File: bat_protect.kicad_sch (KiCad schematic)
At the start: 16 parts, among them Q9 Q_NMOS_DGS, U14 BQ29209DRBR

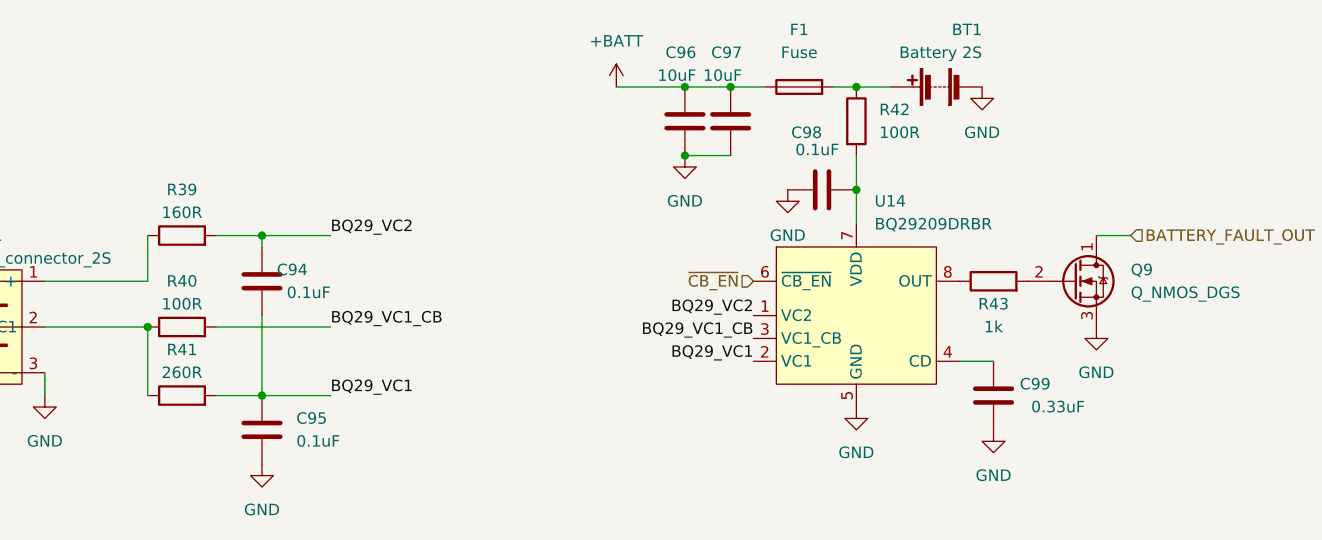
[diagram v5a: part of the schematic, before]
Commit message: datasheet checkout, added couple of capacitors for usb-c, groupd some scheatics
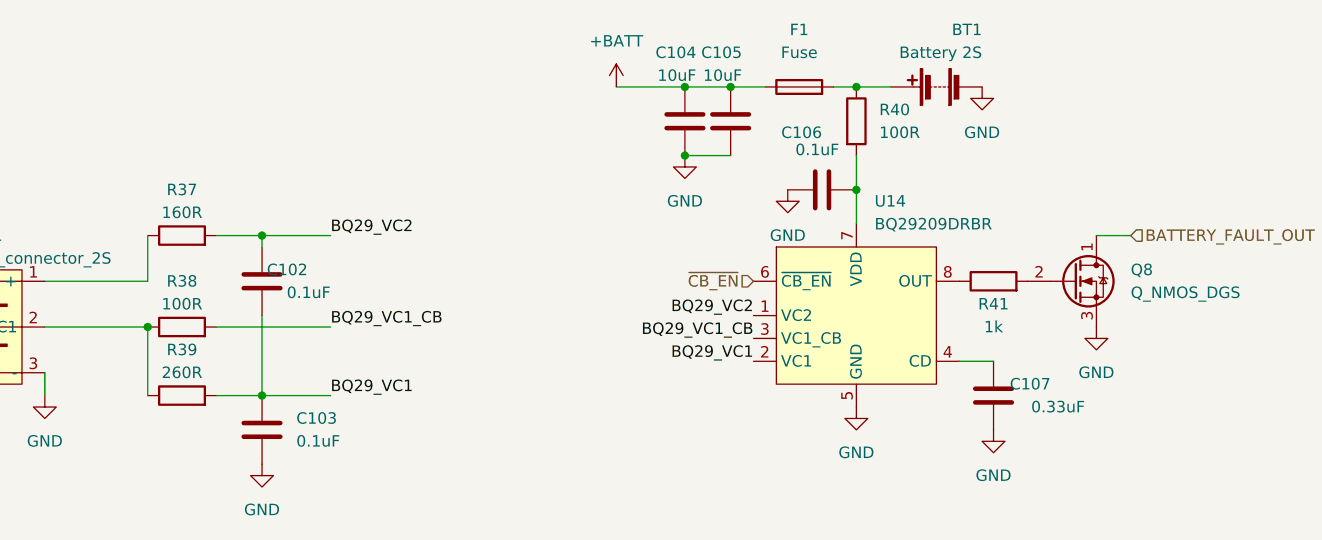
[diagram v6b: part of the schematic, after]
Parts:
- renumbered C94 to C102, C95 to C103, C96 to C104, C97 to C105, C98 to C106, C99 to C107, Q9 to Q8, R39 to R37, R40 to R38, R41 to R39, R42 to R40, R43 to R41
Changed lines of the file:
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@@
   (symbol (lib_id "power:GND") (at 78.74 99.06 0) (unit 1)
     (in_bom yes) (on_board yes) (fields_autoplaced)
-    (property "Reference" "#PWR0117" (id 0) (at 78.74 105.41 0)
+    (property "Reference" "#PWR0118" (id 0) (at 78.74 105.41 0)
       (effects (font (size 1.27 1.27)) hide)
     )
@@
   (symbol (lib_id "Device:R") (at 93.98 91.44 90) (unit 1)
     (in_bom yes) (on_board yes)
-    (property "Reference" "R40" (id 0) (at 93.98 86.36 90))
+    (property "Reference" "R38" (id 0) (at 93.98 86.36 90))
     (property "Value" "100R" (id 1) (at 93.98 88.9 90))
     (property "Footprint" "" (id 2) (at 93.98 93.218 90)
@@
   (symbol (lib_id "power:+BATT") (at 142.24 64.77 0) (unit 1)
     (in_bom yes) (on_board yes) (fields_autoplaced)
-    (property "Reference" "#PWR0119" (id 0) (at 142.24 68.58 0)
+    (property "Reference" "#PWR0120" (id 0) (at 142.24 68.58 0)
       (effects (font (size 1.27 1.27)) hide)
     )
@@
   (symbol (lib_id "power:GND") (at 102.87 106.68 0) (unit 1)
     (in_bom yes) (on_board yes) (fields_autoplaced)
-    (property "Reference" "#PWR0118" (id 0) (at 102.87 113.03 0)
+    (property "Reference" "#PWR0119" (id 0) (at 102.87 113.03 0)
       (effects (font (size 1.27 1.27)) hide)
     )
@@
   (symbol (lib_id "power:GND") (at 168.91 100.33 0) (unit 1)
     (in_bom yes) (on_board yes) (fields_autoplaced)
-    (property "Reference" "#PWR0122" (id 0) (at 168.91 106.68 0)
+    (property "Reference" "#PWR0123" (id 0) (at 168.91 106.68 0)
       (effects (font (size 1.27 1.27)) hide)
     )
@@
   (symbol (lib_id "power:GND") (at 149.86 72.39 0) (unit 1)
     (in_bom yes) (on_board yes) (fields_autoplaced)
-    (property "Reference" "#PWR0120" (id 0) (at 149.86 78.74 0)
+    (property "Reference" "#PWR0121" (id 0) (at 149.86 78.74 0)
       (effects (font (size 1.27 1.27)) hide)
     )
@@
   (symbol (lib_id "power:GND") (at 182.88 64.77 0) (unit 1)
     (in_bom yes) (on_board yes) (fields_autoplaced)
-    (property "Reference" "#PWR0123" (id 0) (at 182.88 71.12 0)
+    (property "Reference" "#PWR0124" (id 0) (at 182.88 71.12 0)
       (effects (font (size 1.27 1.27)) hide)
     )
@@
   (symbol (lib_id "Device:R") (at 93.98 81.28 90) (unit 1)
     (in_bom yes) (on_board yes)
-    (property "Reference" "R39" (id 0) (at 93.98 76.2 90))
+    (property "Reference" "R37" (id 0) (at 93.98 76.2 90))
     (property "Value" "160R" (id 1) (at 93.98 78.74 90))
     (property "Footprint" "" (id 2) (at 93.98 83.058 90)
@@
   (symbol (lib_id "power:GND") (at 161.29 76.2 0) (unit 1)
     (in_bom yes) (on_board yes) (fields_autoplaced)
-    (property "Reference" "#PWR0121" (id 0) (at 161.29 82.55 0)
+    (property "Reference" "#PWR0122" (id 0) (at 161.29 82.55 0)
       (effects (font (size 1.27 1.27)) hide)
     )
@@
   (symbol (lib_id "Device:C") (at 184.15 99.06 0) (mirror x) (unit 1)
     (in_bom yes) (on_board yes)
-    (property "Reference" "C99" (id 0) (at 190.5 97.79 0)
+    (property "Reference" "C107" (id 0) (at 190.5 97.79 0)
       (effects (font (size 1.27 1.27)) (justify right))
     )
@@
   (symbol (lib_id "Device:R") (at 184.15 86.36 90) (unit 1)
     (in_bom yes) (on_board yes)
-    (property "Reference" "R43" (id 0) (at 184.15 88.9 90))
+    (property "Reference" "R41" (id 0) (at 184.15 88.9 90))
     (property "Value" "1k" (id 1) (at 184.15 91.44 90))
     (property "Footprint" "" (id 2) (at 184.15 88.138 90)
@@
   (symbol (lib_id "Device:Q_NMOS_DGS") (at 193.04 86.36 0) (unit 1)
     (in_bom yes) (on_board yes) (fields_autoplaced)
-    (property "Reference" "Q9" (id 0) (at 199.39 85.0899 0)
+    (property "Reference" "Q8" (id 0) (at 199.39 85.0899 0)
       (effects (font (size 1.27 1.27)) (justify left))
     )
@@
   (symbol (lib_id "Device:C") (at 102.87 102.87 0) (mirror y) (unit 1)
     (in_bom yes) (on_board yes)
-    (property "Reference" "C95" (id 0) (at 106.68 101.6 0)
+    (property "Reference" "C103" (id 0) (at 106.68 101.6 0)
       (effects (font (size 1.27 1.27)) (justify right))
     )
@@
   (symbol (lib_id "power:GND") (at 195.58 91.44 0) (unit 1)
     (in_bom yes) (on_board yes) (fields_autoplaced)
-    (property "Reference" "#PWR0125" (id 0) (at 195.58 97.79 0)
+    (property "Reference" "#PWR0126" (id 0) (at 195.58 97.79 0)
       (effects (font (size 1.27 1.27)) hide)
     )
@@
   (symbol (lib_id "power:GND") (at 184.15 102.87 0) (unit 1)
     (in_bom yes) (on_board yes) (fields_autoplaced)
-    (property "Reference" "#PWR0124" (id 0) (at 184.15 109.22 0)
+    (property "Reference" "#PWR0125" (id 0) (at 184.15 109.22 0)
       (effects (font (size 1.27 1.27)) hide)
     )
@@
   (symbol (lib_id "Device:C") (at 149.86 68.58 0) (mirror x) (unit 1)
     (in_bom yes) (on_board yes)
-    (property "Reference" "C96" (id 0) (at 151.13 60.96 0)
+    (property "Reference" "C104" (id 0) (at 151.13 60.96 0)
       (effects (font (size 1.27 1.27)) (justify right))
     )
@@
   (symbol (lib_id "Device:C") (at 154.94 68.58 0) (mirror x) (unit 1)
     (in_bom yes) (on_board yes)
-    (property "Reference" "C97" (id 0) (at 156.21 60.96 0)
+    (property "Reference" "C105" (id 0) (at 156.21 60.96 0)
       (effects (font (size 1.27 1.27)) (justify right))
     )
@@
   (symbol (lib_id "Device:C") (at 165.1 76.2 270) (mirror x) (unit 1)
     (in_bom yes) (on_board yes)
-    (property "Reference" "C98" (id 0) (at 165.1 69.85 90)
+    (property "Reference" "C106" (id 0) (at 165.1 69.85 90)
       (effects (font (size 1.27 1.27)) (justify right))
     )
@@
   (symbol (lib_id "Device:C") (at 102.87 86.36 0) (mirror x) (unit 1)
     (in_bom yes) (on_board yes)
-    (property "Reference" "C94" (id 0) (at 107.95 85.09 0)
+    (property "Reference" "C102" (id 0) (at 107.95 85.09 0)
       (effects (font (size 1.27 1.27)) (justify right))
     )
@@
   (symbol (lib_id "Device:R") (at 93.98 99.06 90) (unit 1)
     (in_bom yes) (on_board yes)
-    (property "Reference" "R41" (id 0) (at 93.98 93.98 90))
+    (property "Reference" "R39" (id 0) (at 93.98 93.98 90))
     (property "Value" "260R" (id 1) (at 93.98 96.52 90))
     (property "Footprint" "" (id 2) (at 93.98 100.838 90)
@@
   (symbol (lib_id "Device:R") (at 168.91 68.58 0) (unit 1)
     (in_bom yes) (on_board yes) (fields_autoplaced)
-    (property "Reference" "R42" (id 0) (at 171.45 67.3099 0)
-      (effects (font (size 1.27 1.27)) (justify left))
-    )
+    (property "Reference" "R40" (id 0) (at 171.45 67.3099 0)
+      (effects (font (size 1.27 1.27)) (justify left))
+    )

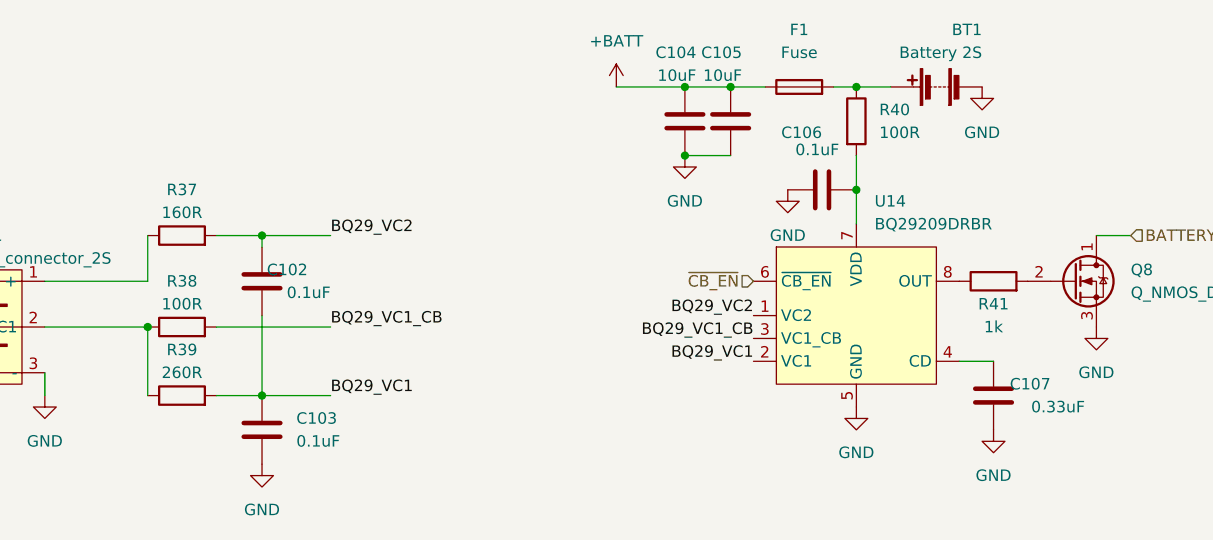
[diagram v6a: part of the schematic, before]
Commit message: added nfc antenna components, added most of footprints
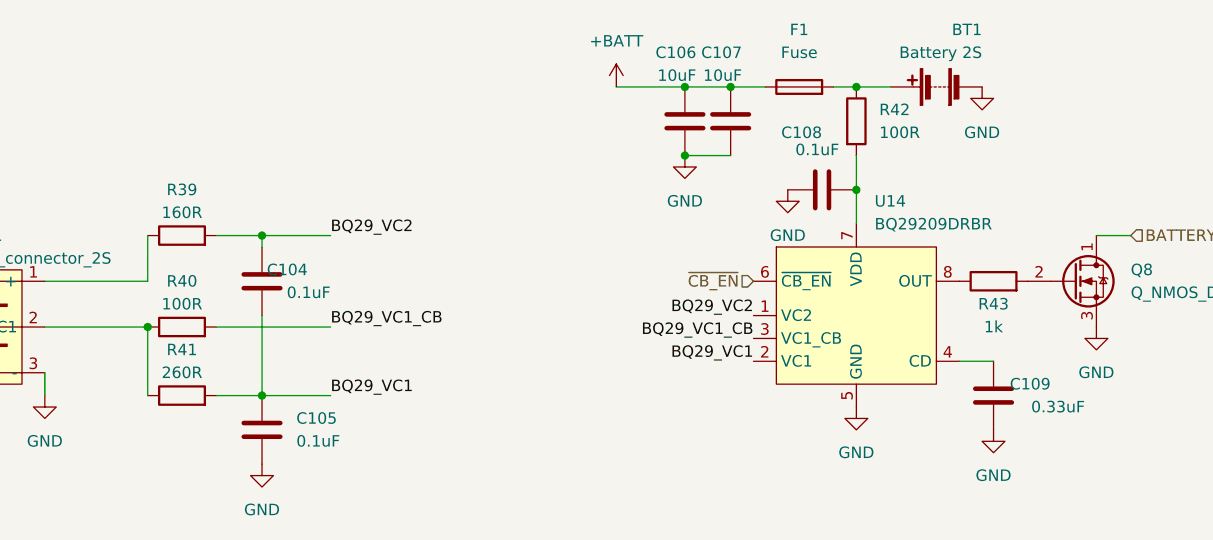
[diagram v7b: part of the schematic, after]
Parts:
- C104: renamed from C102; footprint (none) -> Capacitor_SMD:C_0603_1608Metric_Pad1.08x0.95mm_HandSolder
- C105: renamed from C103; footprint (none) -> Capacitor_SMD:C_0603_1608Metric_Pad1.08x0.95mm_HandSolder
- C108: renamed from C106; footprint (none) -> Capacitor_SMD:C_0603_1608Metric_Pad1.08x0.95mm_HandSolder
- C109: renamed from C107; footprint (none) -> Capacitor_SMD:C_0603_1608Metric_Pad1.08x0.95mm_HandSolder
- R42: renamed from R40; footprint (none) -> Resistor_SMD:R_0603_1608Metric_Pad0.98x0.95mm_HandSolder
- R43: renamed from R41; footprint (none) -> Resistor_SMD:R_0603_1608Metric_Pad0.98x0.95mm_HandSolder
- U14: footprint (none) -> airsoft_controller:VSON-8
- renumbered C104 to C106, C105 to C107, R37 to R39, R38 to R40, R39 to R41
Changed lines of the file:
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@@
   (symbol (lib_id "Device:R") (at 93.98 91.44 90) (unit 1)
     (in_bom yes) (on_board yes)
-    (property "Reference" "R38" (id 0) (at 93.98 86.36 90))
+    (property "Reference" "R40" (id 0) (at 93.98 86.36 90))
     (property "Value" "100R" (id 1) (at 93.98 88.9 90))
     (property "Footprint" "" (id 2) (at 93.98 93.218 90)
@@
   (symbol (lib_id "Device:R") (at 93.98 81.28 90) (unit 1)
     (in_bom yes) (on_board yes)
-    (property "Reference" "R37" (id 0) (at 93.98 76.2 90))
+    (property "Reference" "R39" (id 0) (at 93.98 76.2 90))
     (property "Value" "160R" (id 1) (at 93.98 78.74 90))
     (property "Footprint" "" (id 2) (at 93.98 83.058 90)
@@
   (symbol (lib_id "Device:C") (at 184.15 99.06 0) (mirror x) (unit 1)
     (in_bom yes) (on_board yes)
-    (property "Reference" "C107" (id 0) (at 190.5 97.79 0)
+    (property "Reference" "C109" (id 0) (at 190.5 97.79 0)
       (effects (font (size 1.27 1.27)) (justify right))
     )
@@
       (effects (font (size 1.27 1.27)) (justify right))
     )
-    (property "Footprint" "" (id 2) (at 185.1152 95.25 0)
+    (property "Footprint" "Capacitor_SMD:C_0603_1608Metric_Pad1.08x0.95mm_HandSolder" (id 2) (at 185.1152 95.25 0)
       (effects (font (size 1.27 1.27)) hide)
     )
@@
   (symbol (lib_id "Device:R") (at 184.15 86.36 90) (unit 1)
     (in_bom yes) (on_board yes)
-    (property "Reference" "R41" (id 0) (at 184.15 88.9 90))
+    (property "Reference" "R43" (id 0) (at 184.15 88.9 90))
     (property "Value" "1k" (id 1) (at 184.15 91.44 90))
-    (property "Footprint" "" (id 2) (at 184.15 88.138 90)
+    (property "Footprint" "Resistor_SMD:R_0603_1608Metric_Pad0.98x0.95mm_HandSolder" (id 2) (at 184.15 88.138 90)
       (effects (font (size 1.27 1.27)) hide)
     )
@@
   (symbol (lib_id "Device:C") (at 102.87 102.87 0) (mirror y) (unit 1)
     (in_bom yes) (on_board yes)
-    (property "Reference" "C103" (id 0) (at 106.68 101.6 0)
+    (property "Reference" "C105" (id 0) (at 106.68 101.6 0)
       (effects (font (size 1.27 1.27)) (justify right))
     )
@@
       (effects (font (size 1.27 1.27)) (justify right))
     )
-    (property "Footprint" "" (id 2) (at 101.9048 106.68 0)
+    (property "Footprint" "Capacitor_SMD:C_0603_1608Metric_Pad1.08x0.95mm_HandSolder" (id 2) (at 101.9048 106.68 0)
       (effects (font (size 1.27 1.27)) hide)
     )
@@
   (symbol (lib_id "Device:C") (at 149.86 68.58 0) (mirror x) (unit 1)
     (in_bom yes) (on_board yes)
-    (property "Reference" "C104" (id 0) (at 151.13 60.96 0)
+    (property "Reference" "C106" (id 0) (at 151.13 60.96 0)
       (effects (font (size 1.27 1.27)) (justify right))
     )
@@
   (symbol (lib_id "Device:C") (at 154.94 68.58 0) (mirror x) (unit 1)
     (in_bom yes) (on_board yes)
-    (property "Reference" "C105" (id 0) (at 156.21 60.96 0)
+    (property "Reference" "C107" (id 0) (at 156.21 60.96 0)
       (effects (font (size 1.27 1.27)) (justify right))
     )
@@
   (symbol (lib_id "Device:C") (at 165.1 76.2 270) (mirror x) (unit 1)
     (in_bom yes) (on_board yes)
-    (property "Reference" "C106" (id 0) (at 165.1 69.85 90)
+    (property "Reference" "C108" (id 0) (at 165.1 69.85 90)
       (effects (font (size 1.27 1.27)) (justify right))
     )
@@
       (effects (font (size 1.27 1.27)) (justify right))
     )
-    (property "Footprint" "" (id 2) (at 161.29 75.2348 0)
+    (property "Footprint" "Capacitor_SMD:C_0603_1608Metric_Pad1.08x0.95mm_HandSolder" (id 2) (at 161.29 75.2348 0)
       (effects (font (size 1.27 1.27)) hide)
     )
@@
   (symbol (lib_id "Device:C") (at 102.87 86.36 0) (mirror x) (unit 1)
     (in_bom yes) (on_board yes)
-    (property "Reference" "C102" (id 0) (at 107.95 85.09 0)
+    (property "Reference" "C104" (id 0) (at 107.95 85.09 0)
       (effects (font (size 1.27 1.27)) (justify right))
     )
@@
       (effects (font (size 1.27 1.27)) (justify right))
     )
-    (property "Footprint" "" (id 2) (at 103.8352 82.55 0)
+    (property "Footprint" "Capacitor_SMD:C_0603_1608Metric_Pad1.08x0.95mm_HandSolder" (id 2) (at 103.8352 82.55 0)
       (effects (font (size 1.27 1.27)) hide)
     )
@@
   (symbol (lib_id "Device:R") (at 93.98 99.06 90) (unit 1)
     (in_bom yes) (on_board yes)
-    (property "Reference" "R39" (id 0) (at 93.98 93.98 90))
+    (property "Reference" "R41" (id 0) (at 93.98 93.98 90))
     (property "Value" "260R" (id 1) (at 93.98 96.52 90))
     (property "Footprint" "" (id 2) (at 93.98 100.838 90)
@@
   (symbol (lib_id "Device:R") (at 168.91 68.58 0) (unit 1)
     (in_bom yes) (on_board yes) (fields_autoplaced)
-    (property "Reference" "R40" (id 0) (at 171.45 67.3099 0)
+    (property "Reference" "R42" (id 0) (at 171.45 67.3099 0)
       (effects (font (size 1.27 1.27)) (justify left))
     )
@@
       (effects (font (size 1.27 1.27)) (justify left))
     )
-    (property "Footprint" "" (id 2) (at 167.132 68.58 90)
+    (property "Footprint" "Resistor_SMD:R_0603_1608Metric_Pad0.98x0.95mm_HandSolder" (id 2) (at 167.132 68.58 90)
       (effects (font (size 1.27 1.27)) hide)
     )
@@
       (effects (font (size 1.27 1.27)) (justify left))
     )
-    (property "Footprint" "" (id 2) (at 168.91 90.17 0)
-      (effects (font (size 1.27 1.27)) hide)
-    )
+    (property "Footprint" "airsoft_controller:VSON-8" (id 2) (at 168.91 90.17 0)
+      (effects (font (size 1.27 1.27)) hide)
+    )

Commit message: schematic creation
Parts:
- added Q6: Q_NMOS_DGS, Package_TO_SOT_SMD:SOT-23, symbol Device:Q_NMOS_GSD
- added Q7: Q_NMOS_DGS, Package_TO_SOT_SMD:SOT-23, symbol Device:Q_PMOS_GSD
- added R42: 0R, Resistor_SMD:R_0603_1608Metric_Pad0.98x0.95mm_HandSolder, symbol Device:R
- BT1: footprint (none) -> airsoft_controller:BAT_CONN_5mm_pitch
- C114: renamed from C106; footprint (none) -> Capacitor_SMD:C_1206_3216Metric_Pad1.33x1.80mm_HandSolder
- C115: renamed from C107; footprint (none) -> Capacitor_SMD:C_1206_3216Metric_Pad1.33x1.80mm_HandSolder
- F1: footprint (none) -> airsoft_controller:fuse_clip_5x20-33mm
- JP1: footprint (none) -> airsoft_controller:JST_XH_3P-Horizontal
- Q8: footprint (none) -> Package_TO_SOT_SMD:SOT-23; symbol Device:Q_NMOS_DGS -> Device:Q_NMOS_GSD
- R39, R41: footprint (none) -> Resistor_SMD:R_0603_1608Metric_Pad0.98x0.95mm_HandSolder
- R40: footprint (none) -> Resistor_THT:R_Box_L13.0mm_W4.0mm_P9.00mm
- R43: renamed from R42; footprint Resistor_SMD:R_0603_1608Metric_Pad0.98x0.95mm_HandSolder -> Resistor_THT:R_Box_L13.0mm_W4.0mm_P9.00mm
- renumbered C104 to C110, C105 to C111, C108 to C112, C109 to C113, R43 to R44, U14 to U16
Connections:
- net BATTERY_FAULT_OUT: now also Q8.3 (D); no longer Q8.1 (D)
- net BQ29_VC1_CB: now also Q6.1 (G), Q7.1 (G), R42.2; no longer R40.2
- net GND: now also Q8.2 (S), Q7.3 (D); no longer Q8.3 (S)
- net BAT_CB2: now reaches JP1.1 (+), R39.1
- net BAT_CB2: now also R43.1, Q6.2 (S)
- net at R44.2: now also Q8.1 (G); no longer Q8.2 (G)
- net at BT1.1 (+), F1.2: no longer R43.1
- new net: Q6.3 (D), Q7.2 (S), R40.2, R42.1
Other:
- note added: "I_{bal} = V_{CELL}/R_{CB}"
- note added: "ext balance 0R if no ext R >2k if ext"
- note added: "int balance I_{CB1}= V_{C1} ~{R_{VC1}+R_{VC1_CB}} I_{CB2}= V_{C2}-V_{C1} ~{R_{VC2}+R_{VC1_CB}+R_{VDD}} Supports max 15mA balance"
- moved on the sheet: BT1, C110, C111, C114, C115, F1, JP1, R39, R40, R41
